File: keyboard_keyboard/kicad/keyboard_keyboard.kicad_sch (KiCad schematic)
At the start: 462 parts, among them J1 AudioJack3_Ground, J2 AudioJack3_Ground, J3 Screen Connector, J4 DIN-5, J5 DIN-5, U1 74HC138, U2 6N138

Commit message: fix gnd
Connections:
- net gnd is gone; now on net GND: J4.3
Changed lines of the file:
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@@
 	(wire
 		(pts
+			(xy 935.99 312.42) (xy 941.07 312.42)
+		)
+		(stroke
+			(width 0)
+			(type default)
+		)
+	)
+	(wire
+		(pts
 			(xy 1040.13 130.81) (xy 1040.13 129.54)
 		)
@@
 	(wire
 		(pts
+			(xy 580.39 290.83) (xy 568.96 290.83)
+		)
+		(stroke
+			(width 0)
+			(type default)
+		)
+	)
+	(wire
+		(pts
 			(xy 791.21 92.71) (xy 791.21 93.98)
 		)
@@
 	(wire
 		(pts
+			(xy 941.07 312.42) (xy 941.07 313.69)
+		)
+		(stroke
+			(width 0)
+			(type default)
+		)
+	)
+	(wire
+		(pts
 			(xy 317.5 217.17) (xy 317.5 218.44)
 		)
@@
 		)
 	)
+	(wire
+		(pts
+			(xy 568.96 290.83) (xy 568.96 292.1)
+		)
+		(stroke
+			(width 0)
+			(type default)
+		)
+	)
 	(polyline
 		(pts
@@
 	(wire
 		(pts
-			(xy 935.99 314.96) (xy 935.99 317.5)
+			(xy 935.99 312.42) (xy 935.99 317.5)
 		)
 		(stroke
@@
 		)
 	)
-	(global_label "GND"
-		(shape input)
-		(at 580.39 290.83 180)
-		(fields_autoplaced yes)
-		(effects
-			(font
-				(size 1.27 1.27)
-			)
-			(justify right)
-		)
-		(property "Intersheetrefs" "${INTERSHEET_REFS}"
-			(at 573.5343 290.83 0)
-			(effects
-				(font
-					(size 1.27 1.27)
-				)
-				(justify right)
-				(hide yes)
-			)
-		)
-	)
 	(global_label "MUX_SELECT_2"
 		(shape input)
@@
 		)
 	)
-	(global_label "gnd"
-		(shape input)
-		(at 935.99 314.96 90)
-		(fields_autoplaced yes)
-		(effects
-			(font
-				(size 1.27 1.27)
-			)
-			(justify left)
-		)
-		(property "Intersheetrefs" "${INTERSHEET_REFS}"
-			(at 935.99 308.5278 90)
-			(effects
-				(font
-					(size 1.27 1.27)
-				)
-				(justify left)
-				(hide yes)
-			)
-		)
-	)
 	(global_label "HE97"
 		(shape input)
@@
 	)
 	(symbol
+		(lib_id "power:GND")
+		(at 941.07 313.69 0)
+		(unit 1)
+		(exclude_from_sim no)
+		(in_bom yes)
+		(on_board yes)
+		(dnp no)
+		(fields_autoplaced yes)
+		(property "Reference" "#PWR0309"
+			(at 941.07 320.04 0)
+			(effects
+				(font
+					(size 1.27 1.27)
+				)
+				(hide yes)
+			)
+		)
+		(property "Value" "GND"
+			(at 941.07 318.77 0)
+			(effects
+				(font
+					(size 1.27 1.27)
+				)
+				(hide yes)
+			)
+		)
+		(property "Footprint" ""
+			(at 941.07 313.69 0)
+			(effects
+				(font
+					(size 1.27 1.27)
+				)
+				(hide yes)
+			)
+		)
+		(property "Datasheet" ""
+			(at 941.07 313.69 0)
+			(effects
+				(font
+					(size 1.27 1.27)
+				)
+				(hide yes)
+			)
+		)
+		(property "Description" "Power symbol creates a global label with name \"GND\" , ground"
+			(at 941.07 313.69 0)
+			(effects
+				(font
+					(size 1.27 1.27)
+				)
+				(hide yes)
+			)
+		)
+		(pin "1"
+		)
+		(instances
+			(project "keyboard_keyboard"
+				(path "/a04a08f6-0aff-4526-8b14-085b944c1df1"
+					(reference "#PWR0309")
+					(unit 1)
+				)
+			)
+		)
+	)
+	(symbol
 		(lib_id "Mechanical:MountingHole")
 		(at 196.85 24.13 0)
@@
 					(unit 1)
 				)
+			)
+		)
+	)
+	(symbol
+		(lib_id "power:GND")
+		(at 568.96 292.1 0)
+		(unit 1)
+		(exclude_from_sim no)
+		(in_bom yes)
+		(on_board yes)
+		(dnp no)
+		(fields_autoplaced yes)
+		(property "Reference" "#PWR0308"
+			(at 568.96 298.45 0)
+			(effects
+				(font
+					(size 1.27 1.27)
+				)
+				(hide yes)
+			)
+		)
+		(property "Value" "GND"
+			(at 568.96 297.18 0)
+			(effects
+				(font
+					(size 1.27 1.27)
+				)
+				(hide yes)
+			)
+		)
+		(property "Footprint" ""
+			(at 568.96 292.1 0)
+			(effects
+				(font
+					(size 1.27 1.27)
+				)
+				(hide yes)
+			)
+		)
+		(property "Datasheet" ""
+			(at 568.96 292.1 0)
+			(effects
+				(font
+					(size 1.27 1.27)
+				)
+				(hide yes)
+			)
+		)
+		(property "Description" "Power symbol creates a global label with name \"GND\" , ground"
+			(at 568.96 292.1 0)
+			(effects
+				(font
+					(size 1.27 1.27)
+				)
+				(hide yes)
+			)
+		)
+		(pin "1"
+		)
+		(instances
+			(project "keyboard_keyboard"
+				(path "/a04a08f6-0aff-4526-8b14-085b944c1df1"
+					(reference "#PWR0308")
+					(unit 1)
+				)

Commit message: prepare for fab
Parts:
- added J6: Conn_01x04_Socket, Connector_Molex:Molex_Pico-EZmate_78171-0004_1x04-1MP_P1.20mm_Vertical, symbol Connector:Conn_01x04_Socket
- added J7: Conn_01x04_Socket, Connector_PinSocket_2.54mm:PinSocket_1x04_P2.54mm_Vertical, symbol Connector:Conn_01x04_Socket
- A1, D1, D13, D2, D3, J1, J2, J3, J4, J5, R1, R2, R3, R4, R5, R6, R7, R8, RV1, RV10, RV11, RV12, RV2, RV3, RV4, RV5, RV6, RV7, RV8, RV9, U2: now not fitted; now left out of the parts list
- AM1, AM10, AM11, AM12, AM13, AM14, AM15, AM2, AM3, AM4, AM5, AM6, AM7, AM8, AM9: LCSC (none) -> C7793
- C1, C101, C103, C105, C107, C109, C11, C111, C113, C115, C117, C119, C121, C123, C125, C127, C129, C13, C131, C133, C135, C137, C139, C140, C141, C142, C143, C144, C145, C146, C147, C148, C149, C15, C150, C151, C161, C162, C163, C165, C167, C169, C17, C171, C173, C175, C177, C179, C181, C183, C185, C187, C189, C19, C191, C193, C195, C197, C199, C201, C203, C205, C207, C209, C21, C211, C213, C215, C217, C219, C221, C223, C23, C25, C27, C29, C3, C31, C33, C35, C37, C39, C41, C43, C45, C47, C49, C5, C51, C53, C55, C57, C59, C61, C63, C65, C67, C69, C7, C71, C73, C75, C77, C79, C81, C83, C85, C87, C89, C9, C91, C93, C95, C97, C99: LCSC (none) -> C307331
- C10, C100, C102, C104, C106, C108, C110, C112, C114, C116, C118, C12, C120, C122, C124, C126, C128, C130, C132, C134, C136, C138, C14, C16, C164, C166, C168, C170, C172, C174, C176, C178, C18, C180, C182, C184, C186, C188, C190, C192, C194, C196, C198, C2, C20, C200, C202, C204, C206, C208, C210, C212, C214, C216, C218, C22, C220, C222, C224, C24, C26, C28, C30, C32, C34, C36, C38, C4, C40, C42, C44, C46, C48, C50, C52, C54, C56, C58, C6, C60, C62, C64, C66, C68, C70, C72, C74, C76, C78, C8, C80, C82, C84, C86, C88, C90, C92, C94, C96, C98: LCSC (none) -> C1548
- HE1, HE10, HE100, HE11, HE12, HE13, HE14, HE15, HE16, HE17, HE18, HE19, HE2, HE20, HE21, HE22, HE23, HE24, HE25, HE26, HE27, HE28, HE29, HE3, HE30, HE31, HE32, HE33, HE34, HE35, HE36, HE37, HE38, HE39, HE4, HE40, HE41, HE42, HE43, HE44, HE45, HE46, HE47, HE48, HE49, HE5, HE50, HE51, HE52, HE53, HE54, HE55, HE56, HE57, HE58, HE59, HE6, HE60, HE61, HE62, HE63, HE64, HE65, HE66, HE67, HE68, HE69, HE7, HE70, HE71, HE72, HE73, HE74, HE75, HE76, HE77, HE78, HE79, HE8, HE80, HE81, HE82, HE83, HE84, HE85, HE86, HE87, HE88, HE89, HE9, HE90, HE91, HE92, HE93, HE94, HE95, HE96, HE97, HE98, HE99: LCSC (none) -> C5447698
- MX1, MX10, MX100, MX11, MX12, MX13, MX14, MX15, MX16, MX17, MX18, MX19, MX2, MX20, MX21, MX22, MX23, MX24, MX25, MX26, MX27, MX28, MX29, MX3, MX30, MX31, MX32, MX33, MX34, MX35, MX36, MX37, MX38, MX39, MX4, MX40, MX41, MX42, MX43, MX44, MX45, MX46, MX47, MX48, MX49, MX5, MX50, MX51, MX52, MX53, MX54, MX55, MX56, MX57, MX58, MX59, MX6, MX60, MX61, MX62, MX63, MX64, MX65, MX66, MX67, MX68, MX69, MX7, MX70, MX71, MX72, MX73, MX74, MX75, MX76, MX77, MX78, MX79, MX8, MX80, MX81, MX82, MX83, MX84, MX85, MX86, MX87, MX88, MX89, MX9, MX90, MX91, MX92, MX93, MX94, MX95, MX96, MX97, MX98, MX99: now not fitted
- U1: LCSC (none) -> C5602
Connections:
- net GND: now also J6.1 (Pin_1), J7.1 (Pin_1)
- net D-: now reaches A1.36 (USB_D_-)
- net D-: now also J6.2 (Pin_2), J7.2 (Pin_2)
- net D+: now reaches A1.37 (USB_D_+)
- net D+: now also J6.3 (Pin_3), J7.3 (Pin_3)
- net VIN: now reaches A1.39 (VIN)
- net VIN: now also J6.4 (Pin_4), J7.4 (Pin_4)
- no-connect marks 8 -> 5

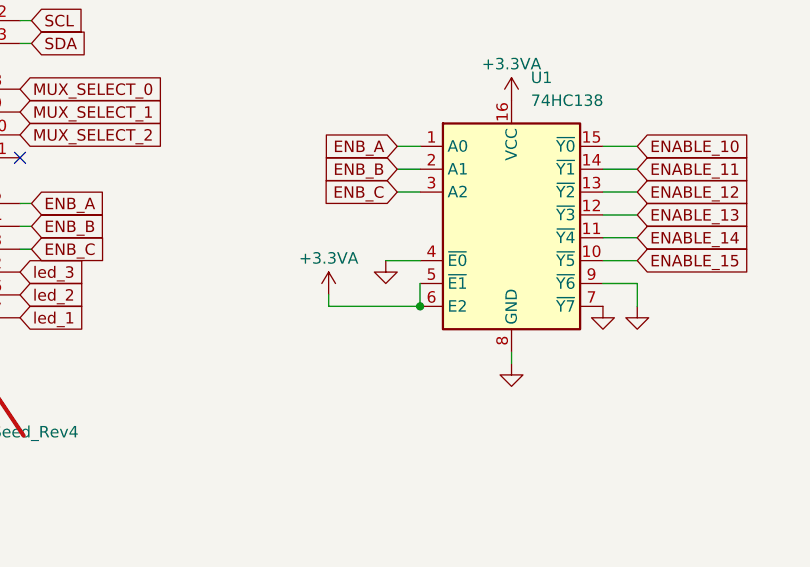
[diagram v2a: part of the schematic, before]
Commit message: fix: mux enable pins wrong
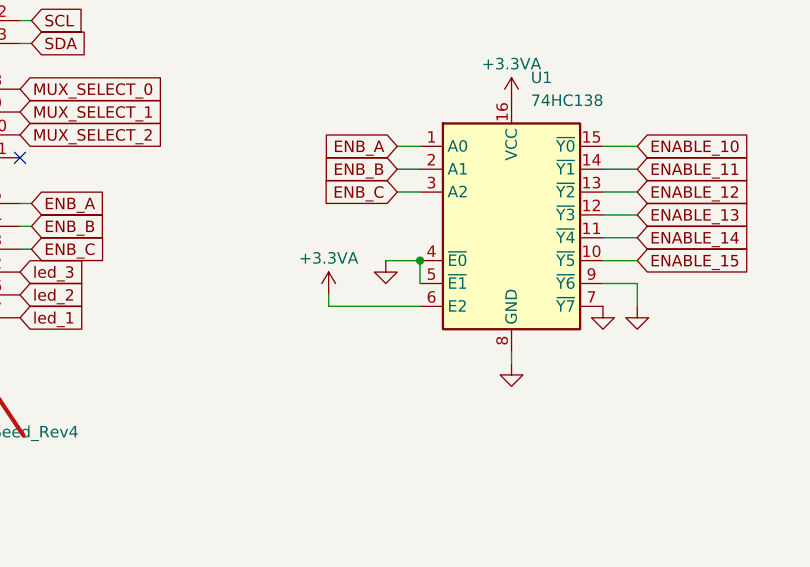
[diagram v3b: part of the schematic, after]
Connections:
- net +3.3VA: no longer U1.5 (~{E1})
- net GND: now also U1.5 (~{E1})
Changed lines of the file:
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@@
 	)
 	(junction
-		(at 759.46 347.98)
-		(diameter 0)
-		(color 0 0 0 0)
-	)
-	(junction
 		(at 400.05 177.8)
 		(diameter 0)
@@
 	)
 	(junction
+		(at 759.46 342.9)
+		(diameter 0)
+		(color 0 0 0 0)
+	)
+	(junction
 		(at 130.81 358.14)
 		(diameter 0)
@@
 	(wire
 		(pts
+			(xy 749.3 347.98) (xy 759.46 347.98)
+		)
+		(stroke
+			(width 0)
+			(type default)
+		)
+	)
+	(wire
+		(pts
 			(xy 447.04 243.84) (xy 452.12 243.84)
 		)
@@
 	(wire
 		(pts
-			(xy 759.46 342.9) (xy 755.65 342.9)
+			(xy 755.65 342.9) (xy 759.46 342.9)
 		)
 		(stroke
@@
 	(wire
 		(pts
-			(xy 749.3 347.98) (xy 759.46 347.98)
-		)
-		(stroke
-			(width 0)
-			(type default)
-		)
-	)
-	(wire
-		(pts
 			(xy 697.23 152.4) (xy 697.23 153.67)
 		)
@@
 	(wire
 		(pts
-			(xy 759.46 347.98) (xy 759.46 345.44)
-		)
-		(stroke
-			(width 0)
-			(type default)
-		)
-	)
-	(wire
-		(pts
 			(xy 985.52 121.92) (xy 985.52 120.65)
 		)
@@
 		)
 		(stroke
+			(width 0)
+			(type default)
+		)
+	)
+	(wire
+		(pts
+			(xy 759.46 345.44) (xy 759.46 342.9)
+		)
+		(stroke

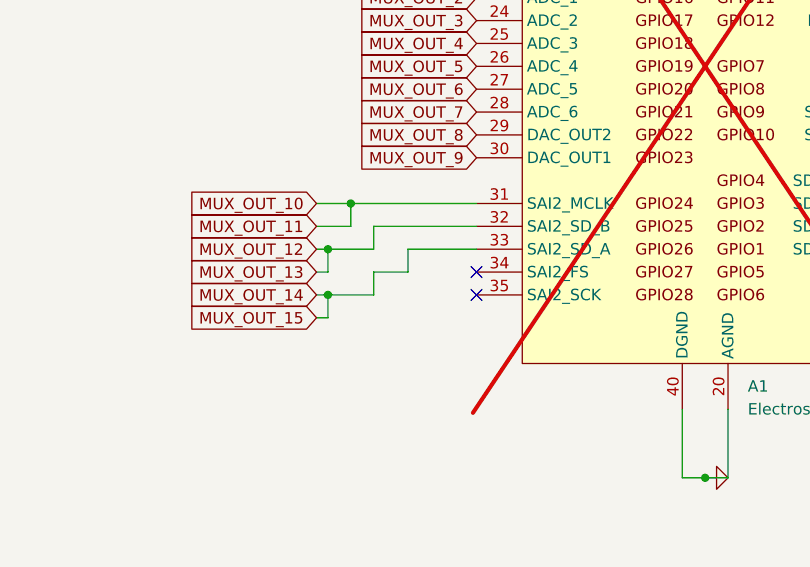
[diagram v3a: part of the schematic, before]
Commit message: feat: wire pots
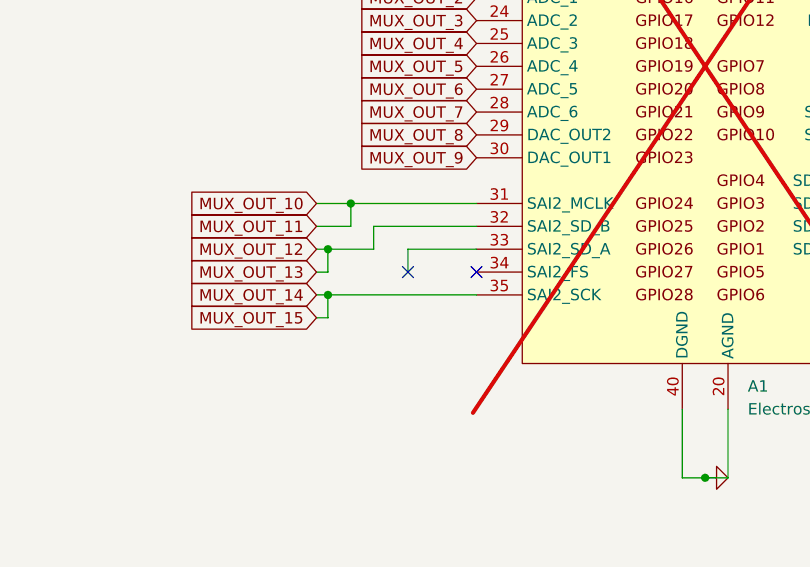
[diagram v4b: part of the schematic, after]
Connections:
- net MUX_OUT_14: now also A1.35 (SAI2_SCK); no longer A1.33 (SAI2_SD_A)
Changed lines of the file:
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@@
 	)
 	(no_connect
-		(at 664.21 349.25)
+		(at 715.01 331.47)
 	)
 	(no_connect
-		(at 715.01 331.47)
+		(at 656.59 346.71)
 	)
 	(no_connect
@@
 	(wire
 		(pts
-			(xy 656.59 346.71) (xy 652.78 346.71)
-		)
-		(stroke
-			(width 0)
-			(type default)
-		)
-	)
-	(wire
-		(pts
 			(xy 814.07 198.12) (xy 819.15 198.12)
 		)
@@
 	(wire
 		(pts
-			(xy 652.78 346.71) (xy 652.78 349.25)
-		)
-		(stroke
-			(width 0)
-			(type default)
-		)
-	)
-	(wire
-		(pts
 			(xy 633.73 105.41) (xy 633.73 106.68)
 		)
@@
 	(wire
 		(pts
-			(xy 652.78 349.25) (xy 647.7 349.25)
-		)
-		(stroke
-			(width 0)
-			(type default)
-		)
-	)
-	(wire
-		(pts
 			(xy 210.82 176.53) (xy 210.82 177.8)
 		)
@@
 		)
 		(stroke
+			(width 0)
+			(type default)
+		)
+	)
+	(wire
+		(pts
+			(xy 647.7 349.25) (xy 664.21 349.25)
+		)
+		(stroke
